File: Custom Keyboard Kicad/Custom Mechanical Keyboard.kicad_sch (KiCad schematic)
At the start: 283 parts, among them J1 USB_C_Receptacle_USB2.0_16P, J2 Conn_01x04_Pin, J3 Conn_01x04_Pin, SW1 SW_SPST, SW10 SW_SPST, SW11 SW_SPST, SW12 SW_SPST, SW13 SW_SPST, SW14 SW_SPST, SW15 SW_SPST, SW16 SW_SPST, SW17 SW_SPST, SW18 SW_SPST, SW19 SW_SPST, SW2 SW_SPST, SW20 SW_SPST, SW21 SW_SPST, SW22 SW_SPST, SW23 SW_SPST, SW24 SW_SPST, SW25 SW_SPST, SW26 SW_SPST, SW27 SW_SPST, SW28 SW_SPST, SW29 SW_SPST, SW3 SW_SPST, SW30 SW_SPST, SW31 SW_SPST, SW32 SW_SPST, SW33 SW_SPST, SW34 SW_SPST, SW35 SW_SPST, SW36 SW_SPST, SW37 SW_SPST, SW38 SW_SPST, SW39 SW_SPST, SW4 SW_SPST, SW40 SW_SPST, SW41 SW_SPST, SW42 SW_SPST, SW43 SW_SPST, SW44 SW_SPST, SW45 SW_SPST, SW46 SW_SPST, SW47 SW_SPST, SW48 SW_SPST, SW49 SW_SPST, SW5 SW_SPST, SW50 SW_SPST, SW51 SW_SPST, SW52 SW_SPST, SW53 SW_SPST, SW54 SW_SPST, SW55 SW_SPST, SW56 SW_SPST, SW57 SW_SPST, SW58 SW_SPST, SW59 SW_SPST, SW6 SW_SPST, SW60 SW_SPST, SW61 SW_SPST, SW62 SW_SPST, SW63 SW_SPST, SW64 SW_SPST, SW65 SW_SPST, SW66 SW_SPST, SW67 SW_SPST, SW68 SW_SPST, SW69 SW_SPST, SW7 SW_SPST, SW70 SW_SPST, SW71 SW_SPST, SW72 SW_SPST, SW73 SW_SPST, SW74 SW_SPST, SW75 SW_SPST, SW76 SW_SPST, SW77 SW_SPST, SW78 SW_SPST, SW79 SW_SPST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

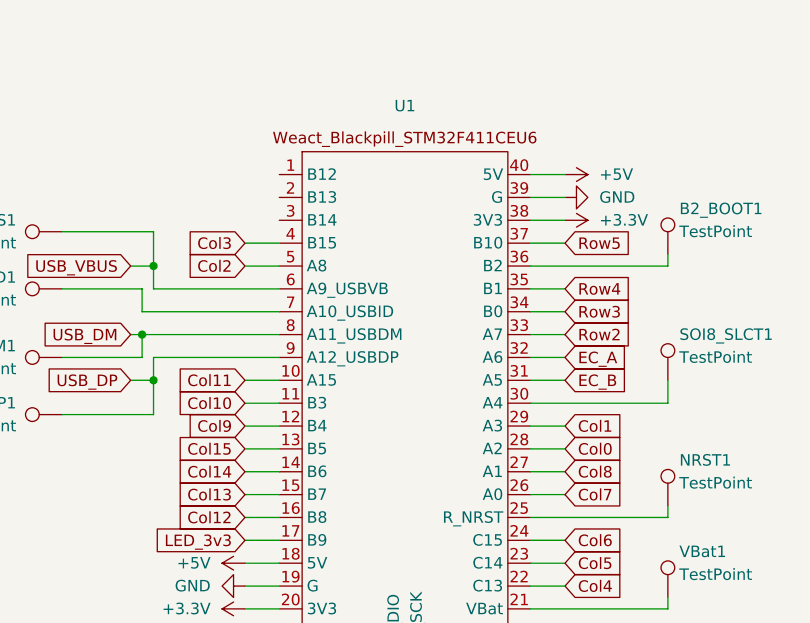
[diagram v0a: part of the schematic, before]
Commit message: Added custom layout json
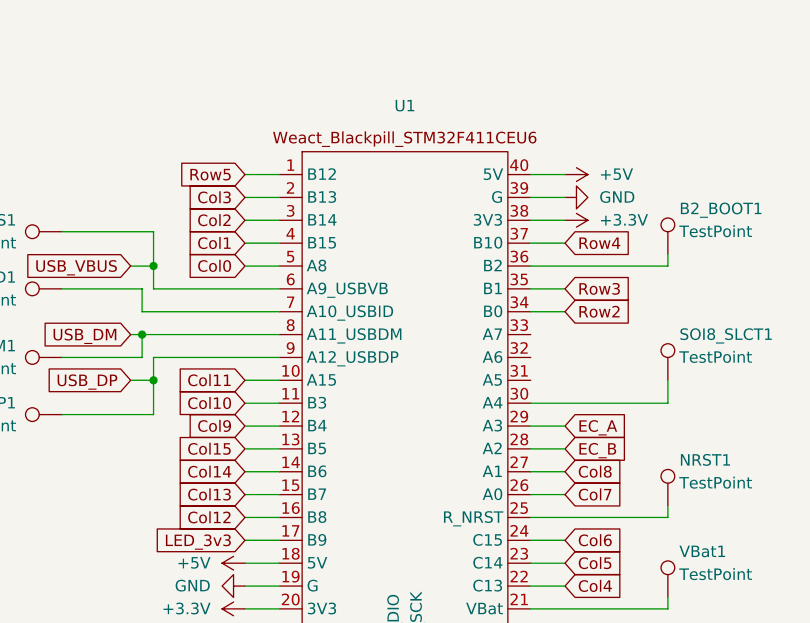
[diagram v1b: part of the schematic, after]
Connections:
- net Col0: now also U1.5 (A8); no longer U1.28 (A2)
- net Col1: now also U1.4 (B15); no longer U1.29 (A3)
- net Col2: now also U1.3 (B14); no longer U1.5 (A8)
- net Col3: now also U1.2 (B13); no longer U1.4 (B15)
- net EC_A: now also U1.29 (A3); no longer U1.32 (A6)
- net EC_B: now also U1.28 (A2); no longer U1.31 (A5)
- net Row2: now also U1.34 (B0); no longer U1.33 (A7)
- net Row3: now also U1.35 (B1); no longer U1.34 (B0)
- net Row4: now also U1.37 (B10); no longer U1.35 (B1)
- net Row5: now also U1.1 (B12); no longer U1.37 (B10)
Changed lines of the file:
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@@
 	(wire
 		(pts
+			(xy 539.75 153.67) (xy 535.94 153.67)
+		)
+		(stroke
+			(width 0)
+			(type default)
+		)
+	)
+	(wire
+		(pts
 			(xy 171.45 332.74) (xy 171.45 330.2)
 		)
@@
 	(wire
 		(pts
+			(xy 504.19 151.13) (xy 508 151.13)
+		)
+		(stroke
+			(width 0)
+			(type default)
+		)
+	)
+	(wire
+		(pts
 			(xy 494.03 242.57) (xy 497.84 242.57)
 		)
@@
 	(wire
 		(pts
-			(xy 535.94 161.29) (xy 539.75 161.29)
-		)
-		(stroke
-			(width 0)
-			(type default)
-		)
-	)
-	(wire
-		(pts
 			(xy 110.49 281.94) (xy 130.81 281.94)
 		)
@@
 	(wire
 		(pts
+			(xy 504.19 153.67) (xy 508 153.67)
+		)
+		(stroke
+			(width 0)
+			(type default)
+		)
+	)
+	(wire
+		(pts
 			(xy 431.8 105.41) (xy 431.8 106.68)
 		)
@@
 	(wire
 		(pts
+			(xy 504.19 146.05) (xy 508 146.05)
+		)
+		(stroke
+			(width 0)
+			(type default)
+		)
+	)
+	(wire
+		(pts
 			(xy 299.72 67.31) (xy 299.72 88.9)
 		)
@@
 	(wire
 		(pts
-			(xy 539.75 173.99) (xy 535.94 173.99)
-		)
-		(stroke
-			(width 0)
-			(type default)
-		)
-	)
-	(wire
-		(pts
 			(xy 199.39 271.78) (xy 204.47 271.78)
 		)
@@
 	(wire
 		(pts
-			(xy 535.94 153.67) (xy 539.75 153.67)
-		)
-		(stroke
-			(width 0)
-			(type default)
-		)
-	)
-	(wire
-		(pts
 			(xy 143.51 246.38) (xy 138.43 246.38)
 		)
@@
 	(wire
 		(pts
-			(xy 59.69 284.48) (xy 59.69 297.18)
+			(xy 539.75 158.75) (xy 535.94 158.75)
 		)
 		(stroke
@@
 	(wire
 		(pts
-			(xy 497.84 242.57) (xy 501.65 242.57)
+			(xy 59.69 284.48) (xy 59.69 297.18)
 		)
 		(stroke
@@
 	(wire
 		(pts
-			(xy 347.98 90.17) (xy 347.98 88.9)
+			(xy 497.84 242.57) (xy 501.65 242.57)
 		)
 		(stroke
@@
 	(wire
 		(pts
-			(xy 246.38 97.79) (xy 246.38 99.06)
+			(xy 347.98 90.17) (xy 347.98 88.9)
 		)
 		(stroke
@@
 	(wire
 		(pts
-			(xy 535.94 163.83) (xy 539.75 163.83)
+			(xy 246.38 97.79) (xy 246.38 99.06)
 		)
 		(stroke
@@
 	(wire
 		(pts
-			(xy 504.19 153.67) (xy 508 153.67)
-		)
-		(stroke
-			(width 0)
-			(type default)
-		)
-	)
-	(wire
-		(pts
 			(xy 339.09 153.67) (xy 340.36 153.67)
 		)
@@
 	(wire
 		(pts
-			(xy 539.75 176.53) (xy 535.94 176.53)
-		)
-		(stroke
-			(width 0)
-			(type default)
-		)
-	)
-	(wire
-		(pts
 			(xy 368.3 76.2) (xy 368.3 77.47)
 		)
@@
 	(wire
 		(pts
+			(xy 504.19 148.59) (xy 508 148.59)
+		)
+		(stroke
+			(width 0)
+			(type default)
+		)
+	)
+	(wire
+		(pts
 			(xy 50.8 36.83) (xy 50.8 39.37)
 		)
@@
 	(wire
 		(pts
+			(xy 539.75 173.99) (xy 535.94 173.99)
+		)
+		(stroke
+			(width 0)
+			(type default)
+		)
+	)
+	(wire
+		(pts
 			(xy 205.74 46.99) (xy 205.74 45.72)
 		)
@@
 	(wire
 		(pts
+			(xy 539.75 161.29) (xy 535.94 161.29)
+		)
+		(stroke
+			(width 0)
+			(type default)
+		)
+	)
+	(wire
+		(pts
 			(xy 165.1 142.24) (xy 185.42 142.24)
 		)
@@
 	(wire
 		(pts
-			(xy 535.94 166.37) (xy 539.75 166.37)
-		)
-		(stroke
-			(width 0)
-			(type default)
-		)
-	)
-	(wire
-		(pts
 			(xy 273.05 236.22) (xy 293.37 236.22)
 		)
@@
 	(wire
 		(pts
-			(xy 535.94 158.75) (xy 539.75 158.75)
-		)
-		(stroke
-			(width 0)
-			(type default)
-		)
-	)
-	(wire
-		(pts
 			(xy 205.74 99.06) (xy 226.06 99.06)
 		)
@@
 	(wire
 		(pts
-			(xy 535.94 168.91) (xy 539.75 168.91)
-		)
-		(stroke
-			(width 0)
-			(type default)
-		)
-	)
-	(wire
-		(pts
 			(xy 245.11 195.58) (xy 240.03 195.58)
 		)
@@
 	(wire
 		(pts
+			(xy 504.19 156.21) (xy 508 156.21)
+		)
+		(stroke
+			(width 0)
+			(type default)
+		)
+	)
+	(wire
+		(pts
 			(xy 63.5 154.94) (xy 63.5 153.67)
 		)
@@
 	(wire
 		(pts
+			(xy 539.75 176.53) (xy 535.94 176.53)
+		)
+		(stroke
+			(width 0)
+			(type default)
+		)
+	)
+	(wire
+		(pts
 			(xy 63.5 132.08) (xy 64.77 132.08)
 		)
@@
 	(wire
 		(pts
-			(xy 504.19 156.21) (xy 508 156.21)
-		)
-		(stroke
-			(width 0)
-			(type default)
-		)
-	)
-	(wire
-		(pts
 			(xy 246.38 55.88) (xy 266.7 55.88)
 		)
@@
 	(global_label "Col2"
 		(shape input)
-		(at 504.19 156.21 180)
+		(at 504.19 151.13 180)
 		(fields_autoplaced yes)
 		(effects
@@
 		)
 		(property "Intersheetrefs" "${INTERSHEET_REFS}"
-			(at 496.9111 156.21 0)
+			(at 496.9111 151.13 0)
 			(effects
 				(font
@@
 	(global_label "Row3"
 		(shape input)
-		(at 539.75 161.29 0)
+		(at 539.75 158.75 0)
 		(fields_autoplaced yes)
 		(effects
@@
 		)
 		(property "Intersheetrefs" "${INTERSHEET_REFS}"
-			(at 547.6942 161.29 0)
+			(at 547.6942 158.75 0)
 			(effects
 				(font
@@
 	(global_label "Col0"
 		(shape input)
-		(at 539.75 176.53 0)
+		(at 504.19 156.21 180)
 		(fields_autoplaced yes)
 		(effects
@@
 				(size 1.27 1.27)
 			)
-			(justify left)
+			(justify right)
 		)
 		(property "Intersheetrefs" "${INTERSHEET_REFS}"
-			(at 547.0289 176.53 0)
+			(at 496.9111 156.21 0)
 			(effects
 				(font
 					(size 1.27 1.27)
 				)
-				(justify left)
+				(justify right)
 				(hide yes)
 			)
@@
 	(global_label "Row4"
 		(shape input)
-		(at 539.75 158.75 0)
+		(at 539.75 153.67 0)
 		(fields_autoplaced yes)
 		(effects
@@
 		)
 		(property "Intersheetrefs" "${INTERSHEET_REFS}"
-			(at 547.6942 158.75 0)
+			(at 547.6942 153.67 0)
 			(effects
 				(font
@@
 	(global_label "EC_B"
 		(shape input)
-		(at 539.75 168.91 0)
+		(at 539.75 176.53 0)
 		(fields_autoplaced yes)
 		(effects
@@
 		)
 		(property "Intersheetrefs" "${INTERSHEET_REFS}"
-			(at 547.3918 168.91 0)
+			(at 547.3918 176.53 0)
 			(effects
 				(font
@@
 	(global_label "EC_A"
 		(shape input)
-		(at 539.75 166.37 0)
+		(at 539.75 173.99 0)
 		(fields_autoplaced yes)
 		(effects
@@
 		)
 		(property "Intersheetrefs" "${INTERSHEET_REFS}"
-			(at 547.2104 166.37 0)
+			(at 547.2104 173.99 0)
 			(effects
 				(font
@@
 	(global_label "Row5"
 		(shape input)
-		(at 539.75 153.67 0)
+		(at 504.19 146.05 180)
 		(fields_autoplaced yes)
 		(effects
@@
 				(size 1.27 1.27)
 			)
-			(justify left)
+			(justify right)
 		)
 		(property "Intersheetrefs" "${INTERSHEET_REFS}"
-			(at 547.6942 153.67 0)
+			(at 496.2458 146.05 0)
 			(effects
 				(font
 					(size 1.27 1.27)
 				)
-				(justify left)
+				(justify right)
 				(hide yes)
 			)
@@
 	(global_label "Col1"
 		(shape input)
-		(at 539.75 173.99 0)
+		(at 504.19 153.67 180)
 		(fields_autoplaced yes)
 		(effects
@@
 				(size 1.27 1.27)
 			)
-			(justify left)
+			(justify right)
 		)
 		(property "Intersheetrefs" "${INTERSHEET_REFS}"
-			(at 547.0289 173.99 0)
+			(at 496.9111 153.67 0)
 			(effects
 				(font
 					(size 1.27 1.27)
 				)
-				(justify left)
+				(justify right)
 				(hide yes)
 			)
@@
 	(global_label "Row2"
 		(shape input)
-		(at 539.75 163.83 0)
+		(at 539.75 161.29 0)
 		(fields_autoplaced yes)
 		(effects
@@
 		)
 		(property "Intersheetrefs" "${INTERSHEET_REFS}"
-			(at 547.6942 163.83 0)
+			(at 547.6942 161.29 0)
 			(effects
 				(font
@@
 	(global_label "Col3"
 		(shape input)
-		(at 504.19 153.67 180)
+		(at 504.19 148.59 180)
 		(fields_autoplaced yes)
 		(effects
@@
 		)
 		(property "Intersheetrefs" "${INTERSHEET_REFS}"
-			(at 496.9111 153.67 0)
+			(at 496.9111 148.59 0)
 			(effects
 				(font

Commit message: Added all ports: USB, display (SPI), BLE (SPI). Fixed all main errors in DRC. Added power switch (linked to power input for board).
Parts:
- removed ESD1: SP0503BAHT, Package_TO_SOT_SMD:SOT-143, symbol Power_Protection:SP0503BAHT
- removed J2, J3: Conn_01x04_Pin, Connector_JST:JST_PH_B4B-PH-K_1x04_P2.00mm_Vertical, symbol Connector:Conn_01x04_Pin
- added J2: Conn_01x04, Connector_JST:JST_PH_B4B-PH-K_1x04_P2.00mm_Vertical, symbol Connector_Generic:Conn_01x04
- added J3: Conn_01x05, Connector_JST:JST_PH_B5B-PH-K_1x05_P2.00mm_Vertical, symbol Connector_Generic:Conn_01x05
- added J4: Conn_01x06, Connector_JST:JST_PH_B6B-PH-K_1x06_P2.00mm_Vertical, symbol Connector_Generic:Conn_01x06
- added J5: Conn_01x07, Connector_JST:JST_PH_B7B-PH-K_1x07_P2.00mm_Vertical, symbol Connector_Generic:Conn_01x07
- added R3, R4: 100k, Resistor_SMD:R_1206_3216Metric_Pad1.30x1.75mm_HandSolder, symbol Device:R
- added SW85: SW_Slide_DPDT, Button_Switch_THT:SW_CK_JS202011AQN_DPDT_Angled, symbol Switch:SW_Slide_DPDT
- added U3: USBLC6-2SC6, Package_TO_SOT_SMD:SOT-23-6, symbol Power_Protection:USBLC6-2SC6
- A10_USB_ID1, A11_USB_DM1, A12_USB_DP1, A9_USB_VBUS1, B2_BOOT1, NRST1, R1, R2, SOI8_SLCT1, VBat1: now left out of the parts list
- CAPS_LED1: value SK6812MINI-E_Rev -> SK6812MINI-E
- D10, D12, D14, D16, D18, D2, D20, D22, D24, D26, D28, D30, D31, D33, D35, D37, D39, D4, D41, D43, D46, D48, D50, D52, D54, D56, D58, D59, D6, D60, D62, D64, D66, D68, D70, D74, D76, D78, D79, D8, D82, D84: value D -> D_Rev; footprint Keyboard_Parts_Footprint:D_SOD123 -> Keyboard_Parts_Footprint:D_SOD123_Rev
- J1: footprint Connector_USB:USB_C_Receptacle_G-Switch_GT-USB-7010ASV -> PCM_marbastlib-various:USB_C_Receptacle_HRO_TYPE-C-31-M-14_(polygon_edge); now left out of the parts list
- renumbered CAPS_D1 to ROT_D1, CAPS_SW1 to ROT_SW1
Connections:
- net +3.3V: now also J4.6 (Pin_6), J5.7 (Pin_7)
- net +5V: now also SW85.2 (B), U3.5 (VBUS)
- net Col0: now also SW18.1 (A), SW2.1 (A), SW33.1 (A), SW48.1 (A), SW62.1 (A), SW76.1 (A), U1.22 (C13); no longer U1.5 (A8)
- net Col1: now also SW19.1 (A), SW20.1 (A), SW3.1 (A), SW34.1 (A), SW35.1 (A), SW4.1 (A), SW49.1 (A), SW50.1 (A), SW63.1 (A), SW64.1 (A), SW77.1 (A), U1.23 (C14); no longer SW18.1 (A), SW2.1 (A), SW33.1 (A), SW48.1 (A), SW62.1 (A), SW76.1 (A), U1.4 (B15)
- net Col2: now also SW21.1 (A), SW22.1 (A), SW36.1 (A), SW37.1 (A), SW5.1 (A), SW51.1 (A), SW52.1 (A), SW6.1 (A), SW65.1 (A), SW66.1 (A), SW78.1 (A), U1.24 (C15); no longer SW19.1 (A), SW3.1 (A), SW34.1 (A), SW49.1 (A), SW63.1 (A), SW77.1 (A), U1.3 (B14)
- net Col3: now also SW23.1 (A), SW24.1 (A), SW38.1 (A), SW39.1 (A), SW53.1 (A), SW54.1 (A), SW67.1 (A), SW68.1 (A), SW7.1 (A), SW8.1 (A), U1.16 (B8); no longer ROT_SW1.S1, SW20.1 (A), SW35.1 (A), SW4.1 (A), SW50.1 (A), SW64.1 (A), U1.2 (B13)
- net Col4: now also SW10.1 (A), SW25.1 (A), SW26.1 (A), SW40.1 (A), SW41.1 (A), SW55.1 (A), SW56.1 (A), SW69.1 (A), SW70.1 (A), SW79.1 (A), SW9.1 (A), U1.15 (B7); no longer SW21.1 (A), SW36.1 (A), SW5.1 (A), SW51.1 (A), SW65.1 (A), U1.22 (C13)
- net Col5: now also SW11.1 (A), SW12.1 (A), SW27.1 (A), SW28.1 (A), SW42.1 (A), SW43.1 (A), SW57.1 (A), SW58.1 (A), SW71.1 (A), SW80.1 (A), U1.14 (B6); no longer SW22.1 (A), SW37.1 (A), SW52.1 (A), SW6.1 (A), SW66.1 (A), SW78.1 (A), U1.23 (C14)
- net Col6: now also SW13.1 (A), SW14.1 (A), SW29.1 (A), SW30.1 (A), SW44.1 (A), SW59.1 (A), SW72.1 (A), SW81.1 (A), SW82.1 (A), U1.13 (B5); no longer SW23.1 (A), SW38.1 (A), SW53.1 (A), SW67.1 (A), SW7.1 (A), U1.24 (C15)
- net Col7: now also ROT_SW1.S1, SW15.1 (A), SW16.1 (A), SW31.1 (A), SW45.1 (A), SW46.1 (A), SW60.1 (A), SW73.1 (A), SW74.1 (A), SW83.1 (A), SW84.1 (A), U1.12 (B4); no longer SW24.1 (A), SW39.1 (A), SW54.1 (A), SW68.1 (A), SW8.1 (A), U1.26 (A0)
- net DM: now also J2.3 (Pin_3)
- net DP: now also J2.2 (Pin_2)
- net EC_A: now also U1.35 (B1); no longer U1.29 (A3)
- net EC_B: now also U1.34 (B0); no longer U1.28 (A2)
- net GND: now also J3.1 (Pin_1), J4.1 (Pin_1), J5.1 (Pin_1), R4.2, SW85.1 (A), SW85.6 (C), U3.2 (GND)
- net Row0: now also D10.2 (A), D12.2 (A), D14.2 (A), D16.2 (A), D2.2 (A), D4.2 (A), D6.2 (A), D8.2 (A); no longer D10.1 (K), D12.1 (K), D14.1 (K), D16.1 (K), D2.1 (K), D4.1 (K), D6.1 (K), D8.1 (K)
- net Row1: now also D18.2 (A), D20.2 (A), D22.2 (A), D24.2 (A), D26.2 (A), D28.2 (A), D30.2 (A), D31.2 (A), ROT_D1.1 (K); no longer D18.1 (K), D20.1 (K), D22.1 (K), D24.1 (K), D26.1 (K), D28.1 (K), D30.1 (K), D31.1 (K)
- net Row2: now also D33.2 (A), D35.2 (A), D37.2 (A), D39.2 (A), D41.2 (A), D43.2 (A), D46.2 (A), U1.26 (A0); no longer D33.1 (K), D35.1 (K), D37.1 (K), D39.1 (K), D41.1 (K), D43.1 (K), D46.1 (K), U1.34 (B0)
- net Row3: now also D48.2 (A), D50.2 (A), D52.2 (A), D54.2 (A), D56.2 (A), D58.2 (A), D59.2 (A), D60.2 (A), U1.27 (A1); no longer D48.1 (K), D50.1 (K), D52.1 (K), D54.1 (K), D56.1 (K), D58.1 (K), D59.1 (K), D60.1 (K), U1.35 (B1)
- net Row4: now also D62.2 (A), D64.2 (A), D66.2 (A), D68.2 (A), D70.2 (A), D74.2 (A), U1.28 (A2); no longer D62.1 (K), D64.1 (K), D66.1 (K), D68.1 (K), D70.1 (K), D74.1 (K), U1.37 (B10)
- net Row5: now also D76.2 (A), D78.2 (A), D79.2 (A), D82.2 (A), D84.2 (A), U1.37 (B10); no longer D76.1 (K), D78.1 (K), D79.1 (K), D82.1 (K), D84.1 (K), ROT_D1.1 (K), U1.1 (B12)
- net USB_DM: now also U3.6 (I/O1)
- net USB_DP: now also U3.4 (I/O2)
- net USB_GND: now also J2.1 (Pin_1)
- net VBUS: now also J2.4 (Pin_4)
- net at SW31.2 (B): now also D31.1 (K); no longer D31.2 (A)
- net at SW39.2 (B): now also D39.1 (K); no longer D39.2 (A)
- net at SW4.2 (B): now also D4.1 (K); no longer D4.2 (A)
- net at SW48.2 (B): now also D48.1 (K); no longer D48.2 (A)
- net at SW22.2 (B): now also D22.1 (K); no longer D22.2 (A)
- net at SW79.2 (B): now also D79.1 (K); no longer D79.2 (A)
- net at SW37.2 (B): now also D37.1 (K); no longer D37.2 (A)
- net at SW60.2 (B): now also D60.1 (K); no longer D60.2 (A)
- net at SW78.2 (B): now also D78.1 (K); no longer D78.2 (A)
- net at SW76.2 (B): now also D76.1 (K); no longer D76.2 (A)
- net at SW35.2 (B): now also D35.1 (K); no longer D35.2 (A)
- net at SW62.2 (B): now also D62.1 (K); no longer D62.2 (A)
- net at SW43.2 (B): now also D43.1 (K); no longer D43.2 (A)
- net at SW28.2 (B): now also D28.1 (K); no longer D28.2 (A)
- net at SW59.2 (B): now also D59.1 (K); no longer D59.2 (A)
- net at SW20.2 (B): now also D20.1 (K); no longer D20.2 (A)
- net at SW2.2 (B): now also D2.1 (K); no longer D2.2 (A)
- net at SW12.2 (B): now also D12.1 (K); no longer D12.2 (A)
- net at SW41.2 (B): now also D41.1 (K); no longer D41.2 (A)
- net at SW64.2 (B): now also D64.1 (K); no longer D64.2 (A)
- net at SW56.2 (B): now also D56.1 (K); no longer D56.2 (A)
- net at SW24.2 (B): now also D24.1 (K); no longer D24.2 (A)
- net at SW18.2 (B): now also D18.1 (K); no longer D18.2 (A)
- net at SW68.2 (B): now also D68.1 (K); no longer D68.2 (A)
- net at SW54.2 (B): now also D54.1 (K); no longer D54.2 (A)
- net at SW33.2 (B): now also D33.1 (K); no longer D33.2 (A)
- net at SW70.2 (B): now also D70.1 (K); no longer D70.2 (A)
- net at SW14.2 (B): now also D14.1 (K); no longer D14.2 (A)
- net at SW6.2 (B): now also D6.1 (K); no longer D6.2 (A)
- net at SW50.2 (B): now also D50.1 (K); no longer D50.2 (A)
- net at SW84.2 (B): now also D84.1 (K); no longer D84.2 (A)
- net at SW30.2 (B): now also D30.1 (K); no longer D30.2 (A)
- net at SW16.2 (B): now also D16.1 (K); no longer D16.2 (A)
- net at SW52.2 (B): now also D52.1 (K); no longer D52.2 (A)
- net at SW82.2 (B): now also D82.1 (K); no longer D82.2 (A)
- net at SW66.2 (B): now also D66.1 (K); no longer D66.2 (A)
- net at SW58.2 (B): now also D58.1 (K); no longer D58.2 (A)
- net at SW10.2 (B): now also D10.1 (K); no longer D10.2 (A)
- net at SW74.2 (B): now also D74.1 (K); no longer D74.2 (A)
- net at SW26.2 (B): now also D26.1 (K); no longer D26.2 (A)
- net at SW46.2 (B): now also D46.1 (K); no longer D46.2 (A)
- net DIS_SCK: now reaches U1.31 (A5)
- net DIS_SCK: now also J5.6 (Pin_6)
- net DIS_MOSI: now reaches U1.33 (A7)
- net DIS_MOSI: now also J5.5 (Pin_5)
- net at SW8.2 (B): now also D8.1 (K); no longer D8.2 (A)
- removed net Col10: SW11.1 (A), SW27.1 (A), SW42.1 (A), SW57.1 (A), SW71.1 (A), SW80.1 (A), U1.11 (B3)
- removed net Col11: SW12.1 (A), SW28.1 (A), SW43.1 (A), SW58.1 (A), U1.10 (A15)
- removed net Col12: SW13.1 (A), SW29.1 (A), SW44.1 (A), SW72.1 (A), SW81.1 (A), U1.16 (B8)
- removed net Col13: SW14.1 (A), SW30.1 (A), SW59.1 (A), SW82.1 (A), U1.15 (B7)
- removed net Col14: SW15.1 (A), SW45.1 (A), SW73.1 (A), SW83.1 (A), U1.14 (B6)
- removed net Col15: SW16.1 (A), SW31.1 (A), SW46.1 (A), SW60.1 (A), SW74.1 (A), SW84.1 (A), U1.13 (B5)
- removed net Col8: SW25.1 (A), SW40.1 (A), SW55.1 (A), SW69.1 (A), SW9.1 (A), U1.27 (A1)
- removed net Col9: SW10.1 (A), SW26.1 (A), SW41.1 (A), SW56.1 (A), SW70.1 (A), SW79.1 (A), U1.12 (B4)
- new net: R3.1, SW85.5 (B)
- new net 5V_IN: J3.5 (Pin_5), SW85.3 (C)
- new net BLE_MISO: J4.4 (Pin_4), U1.3 (B14)
- new net BLE_MOSI: J4.5 (Pin_5), U1.4 (B15)
- new net BLE_SCK: J4.3 (Pin_3), U1.2 (B13)
- new net BLE_SS: J4.2 (Pin_2), U1.1 (B12)
- new net Bat: R3.2, R4.1, U1.29 (A3)
- new net Bat_Sense_IN: J3.2 (Pin_2), SW85.4 (A)
- new net DIS_CS: J5.4 (Pin_4), U1.10 (A15)
- new net DIS_DC: J5.3 (Pin_3), U1.11 (B3)
- new net DIS_RST: J5.2 (Pin_2), U1.5 (A8)
- new net DM_IN: J3.4 (Pin_4), U3.1 (I/O1)
- new net DP_IN: J3.3 (Pin_3), U3.3 (I/O2)
- no-connect marks 3 -> 4
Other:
- moved on the sheet: A10_USB_ID1, A11_USB_DM1, A12_USB_DP1, A9_USB_VBUS1, B2_BOOT1, J1, NRST1, R1, R2, SOI8_SLCT1, U1, VBat1

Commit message: Commit before export
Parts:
- removed NRST1: TestPoint, TestPoint:TestPoint_Pad_D1.0mm, symbol Connector:TestPoint
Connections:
- no-connect marks 4 -> 5
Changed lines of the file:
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@@
 	)
 	(no_connect
+		(at 535.94 161.29)
+	)
+	(no_connect
 		(at 382.27 322.58)
 	)
@@
 	(wire
 		(pts
-			(xy 551.18 160.02) (xy 551.18 161.29)
-		)
-		(stroke
-			(width 0)
-			(type default)
-		)
-	)
-	(wire
-		(pts
 			(xy 279.4 110.49) (xy 278.13 110.49)
 		)
@@
 	(wire
 		(pts
-			(xy 535.94 161.29) (xy 551.18 161.29)
-		)
-		(stroke
-			(width 0)
-			(type default)
-		)
-	)
-	(wire
-		(pts
 			(xy 273.05 307.34) (xy 313.69 307.34)
 		)
@@
 		(exclude_from_sim no)
 		(in_bom no)
-		(on_board no)
+		(on_board yes)
 		(dnp no)
 		(property "Reference" "J2"
@@
 		(exclude_from_sim no)
 		(in_bom no)
-		(on_board no)
+		(on_board yes)
 		(dnp no)
 		(property "Reference" "R2"
@@
 	)
 	(symbol
-		(lib_id "Connector:TestPoint")
-		(at 551.18 160.02 0)
-		(unit 1)
-		(exclude_from_sim no)
-		(in_bom no)
-		(on_board yes)
-		(dnp no)
-		(property "Reference" "NRST1"
-			(at 552.45 154.94 0)
-			(effects
-				(font
-					(size 1.27 1.27)
-				)
-				(justify left)
-			)
-		)
-		(property "Value" "TestPoint"
-			(at 552.45 157.48 0)
-			(effects
-				(font
-					(size 1.27 1.27)
-				)
-				(justify left)
-			)
-		)
-		(property "Footprint" "TestPoint:TestPoint_Pad_D1.0mm"
-			(at 556.26 160.02 0)
-			(effects
-				(font
-					(size 1.27 1.27)
-				)
-				(hide yes)
-			)
-		)
-		(property "Datasheet" "~"
-			(at 556.26 160.02 0)
-			(effects
-				(font
-					(size 1.27 1.27)
-				)
-				(hide yes)
-			)
-		)
-		(property "Description" "test point"
-			(at 551.18 160.02 0)
-			(effects
-				(font
-					(size 1.27 1.27)
-				)
-				(hide yes)
-			)
-		)
-		(pin "1"
-		)
-		(instances
-			(project ""
-				(path "/bf85d36b-b543-4af2-8831-9827a94ddedd"
-					(reference "NRST1")
-					(unit 1)
-				)
-			)
-		)
-	)
-	(symbol
 		(lib_id "LED_SMD:SK6812MINI-E")
 		(at 273.05 246.38 0)
@@
 		(exclude_from_sim no)
 		(in_bom no)
-		(on_board no)
+		(on_board yes)
 		(dnp no)
 		(property "Reference" "R1"
